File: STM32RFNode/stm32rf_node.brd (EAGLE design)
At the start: 100 x 80 mm, 6 parts

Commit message: rounting step 1
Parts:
- U$2: value NRF24L01+REFDESIGN -> NRF24L01+REFDESIGNMINI; device nRF24L01+RefDesign:NRF24L01+REFDESIGN -> nRF24L01+RefDesign:NRF24L01+REFDESIGN-MINI
- moved U$5 24.3 mm to (47.0, 11.4), flipped to the bottom, turned to 270 degrees
- moved U$4 23.4 mm to (22.9, 8.89), flipped to the bottom, turned to 270 degrees
- moved U$3 23.3 mm to (38.1, 8.89), flipped to the bottom, turned to 270 degrees
- moved U$2 4.02 mm to (12.7, 10.2)
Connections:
- new net INT: U$1.PB_0, U$4.INT
- new net N$11: U$1.PC_15, U$2.3
- net N$1: now also U$1.PA_7, U$2.6; no longer U$1.PB_14, U$2.7
- net N$2: now also U$1.PA_6, U$2.7; no longer U$1.PB_15, U$2.6
- net N$3: now also U$1.PA_5; no longer U$1.PB_13
- net N$4: now also U$1.PA_4; no longer U$1.PB_12
- net N$5: now also U$1.PB_1, U$4.A0; no longer U$1.PA_8, U$2.3
- net N$6: now also U$1.PA_0; no longer U$1.PA_9
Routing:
- net GND: track 0.00 -> 58.9 mm
- net N$5: track 0.00 -> 13.3 mm
- net N$3: track 0.00 -> 13.2 mm
- net 3V3: track 0.00 -> 11.2 mm
- net 5V: track 0.00 -> 8.67 mm
- net INT: track 0.00 -> 6.17 mm
- net N$6: track 0.00 -> 5.08 mm
- net N$8: track 0.00 -> 2.54 mm
- net N$7: track 0.00 -> 2.54 mm

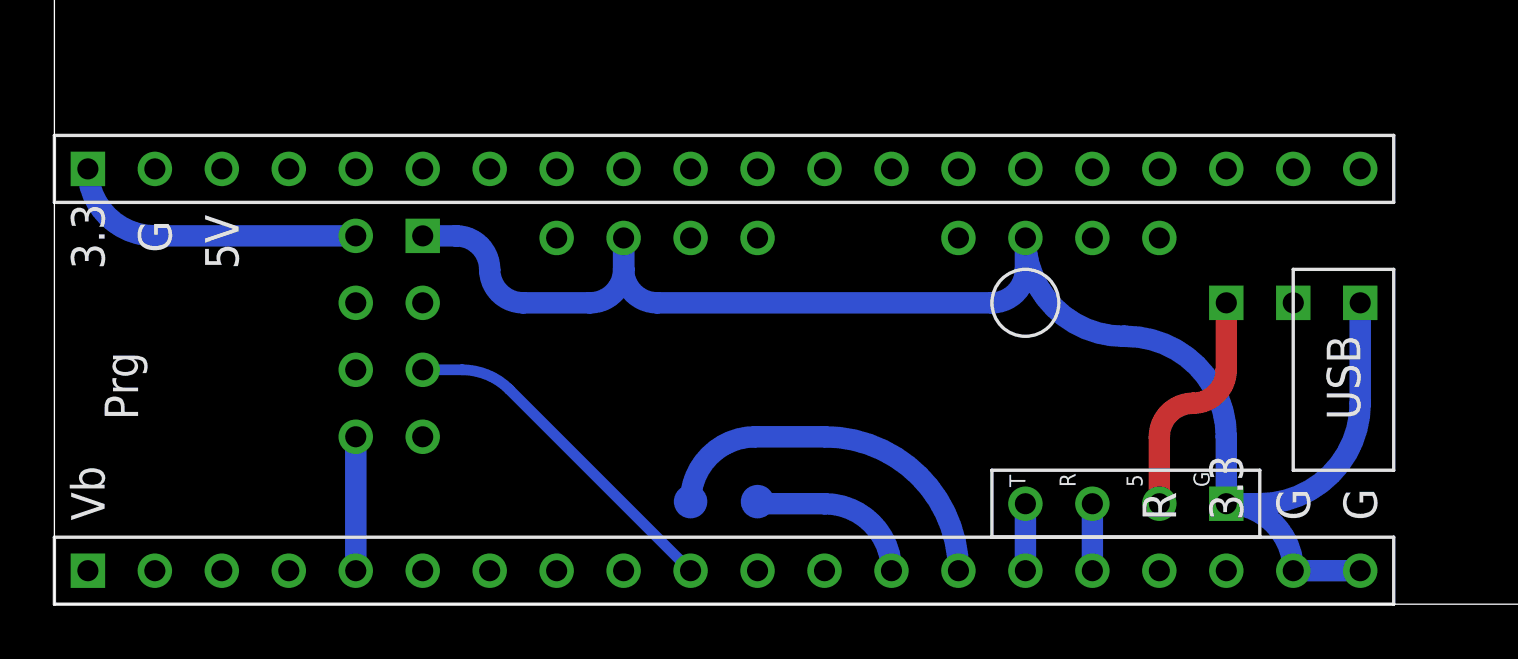
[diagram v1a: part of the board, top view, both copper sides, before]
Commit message: done routing with gnd rastnet
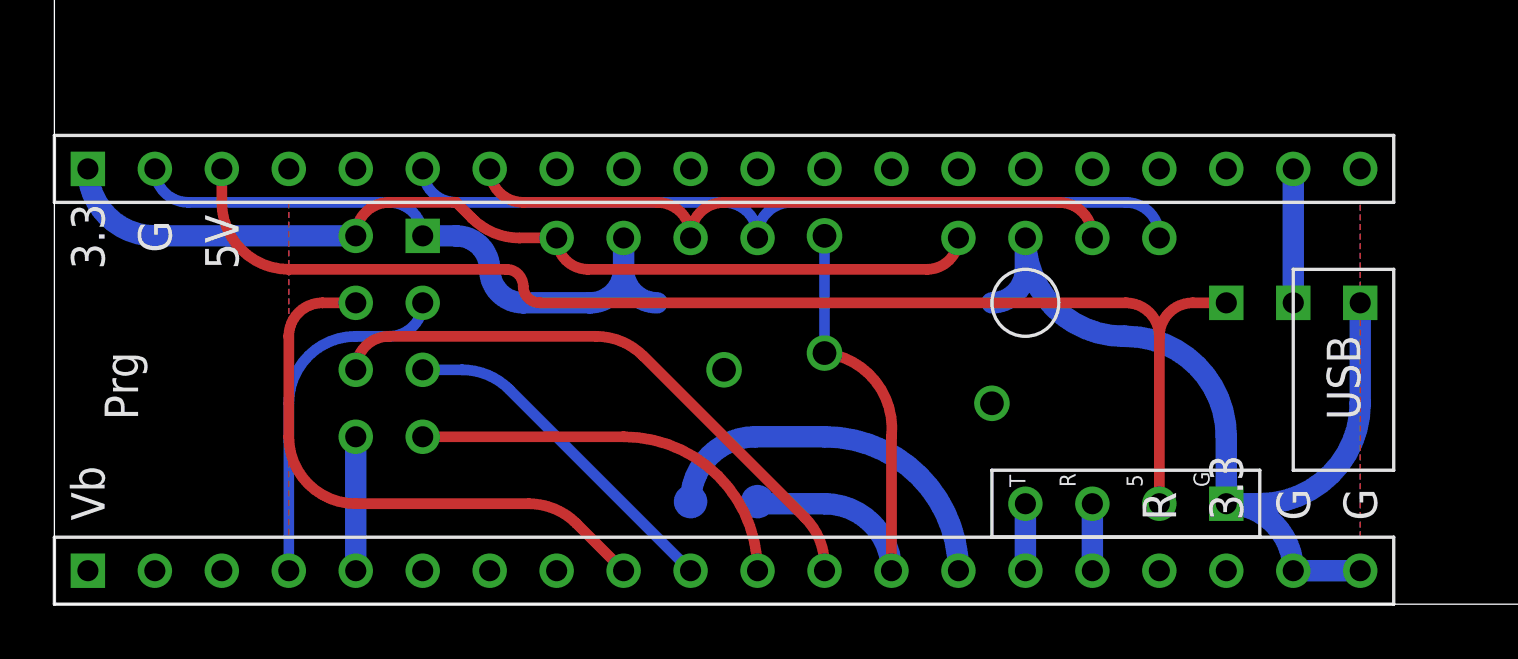
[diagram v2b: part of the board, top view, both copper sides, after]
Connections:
- new net N$12: U$1.PB_13, U$5.S
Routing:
- net 5V: track 8.67 -> 48.4 mm
- net N$10: track 0.00 -> 30.3 mm
- net N$9: track 0.00 -> 25.2 mm
- net 3V3: track 11.2 -> 36.0 mm
- net N$1: track 0.00 -> 22.4 mm
- net N$4: track 0.00 -> 21.5 mm
- net N$2: track 0.00 -> 14.8 mm
- net INT: track 6.17 -> 19.8 mm, vias 0 -> 2
- net N$11: track 0.00 -> 13.0 mm
- net N$12: track 0.00 -> 5.08 mm
- net GND: track 58.9 -> 56.3 mm, vias 0 -> 2
- added copper zone on layer 1, net GND
- added copper zone on layer 16, net GND
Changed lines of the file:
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@@
 <wire x1="36.83" y1="13.89" x2="36.83" y2="12.7" width="0.8128" layer="16"/>
 <wire x1="36.83" y1="12.7" x2="35.56" y2="11.43" width="0.8128" layer="16" curve="-90"/>
-<wire x1="35.56" y1="11.43" x2="22.86" y2="11.43" width="0.8128" layer="16"/>
 <wire x1="22.86" y1="11.43" x2="21.59" y2="12.7" width="0.8128" layer="16" curve="-90"/>
-<wire x1="21.59" y1="12.7" x2="21.59" y2="13.89" width="0.8128" layer="16"/>
 <wire x1="21.59" y1="13.89" x2="21.59" y2="12.7" width="0.8128" layer="16"/>
 <wire x1="21.59" y1="12.7" x2="20.32" y2="11.43" width="0.8128" layer="16" curve="-90"/>
@@
 <wire x1="16.51" y1="12.7" x2="15.24" y2="13.97" width="0.8128" layer="16" curve="90"/>
 <wire x1="15.24" y1="13.97" x2="13.97" y2="13.97" width="0.8128" layer="16"/>
-<wire x1="3.81" y1="16.51" x2="13.97" y2="13.97" width="0" layer="19" extent="1-1"/>
+<wire x1="13.97" y1="13.97" x2="12.7" y2="15.24" width="0.4064" layer="16" curve="90"/>
+<wire x1="12.7" y1="15.24" x2="5.08" y2="15.24" width="0.4064" layer="16"/>
+<wire x1="5.08" y1="15.24" x2="3.81" y2="16.51" width="0.4064" layer="16" curve="-90"/>
+<polygon width="0.4064" layer="16" isolate="0.8128">
+<vertex x="8.89" y="15.24"/>
+<vertex x="8.89" y="2.54"/>
+<vertex x="49.53" y="2.54"/>
+<vertex x="49.53" y="15.24"/>
+</polygon>
+<polygon width="0.4064" layer="1" isolate="0.8128">
+<vertex x="8.89" y="15.24"/>
+<vertex x="8.89" y="2.54"/>
+<vertex x="49.53" y="2.54"/>
+<vertex x="49.53" y="15.24"/>
+</polygon>
+<via x="35.56" y="7.62" extent="1-16" drill="0.9"/>
+<via x="25.4" y="8.89" extent="1-16" drill="0.9"/>
 </signal>
 <signal name="3V3">
@@
 <wire x1="11.43" y1="13.97" x2="3.81" y2="13.97" width="0.8128" layer="16"/>
 <wire x1="3.81" y1="13.97" x2="1.27" y2="16.51" width="0.8128" layer="16" curve="-90"/>
-<wire x1="19.05" y1="13.89" x2="34.29" y2="13.89" width="0" layer="19" extent="1-1"/>
-<wire x1="11.43" y1="13.97" x2="19.05" y2="13.89" width="0" layer="19" extent="1-1"/>
+<wire x1="11.43" y1="13.97" x2="12.7" y2="15.24" width="0.4064" layer="1" curve="-90"/>
+<wire x1="12.7" y1="15.24" x2="15.24" y2="15.24" width="0.4064" layer="1"/>
+<wire x1="15.24" y1="15.24" x2="15.84605" y2="14.63395" width="0.4064" layer="1"/>
+<wire x1="15.84605" y1="14.63395" x2="17.642103125" y2="13.89" width="0.4064" layer="1" curve="45.00007"/>
+<wire x1="17.642103125" y1="13.89" x2="19.05" y2="13.89" width="0.4064" layer="1"/>
+<wire x1="19.05" y1="13.89" x2="20.24" y2="12.7" width="0.4064" layer="1" curve="90"/>
+<wire x1="33.1" y1="12.7" x2="34.29" y2="13.89" width="0.4064" layer="1" curve="90"/>
+<wire x1="20.24" y1="12.7" x2="33.1" y2="12.7" width="0.4064" layer="1"/>
 </signal>
 <signal name="5V">
@@
 <contactref element="U$6" pad="2"/>
 <contactref element="U$1" pad="5V"/>
-<wire x1="41.91" y1="3.81" x2="41.91" y2="6.35" width="0.8128" layer="1"/>
-<wire x1="41.91" y1="6.35" x2="43.18" y2="7.62" width="0.8128" layer="1" curve="-90"/>
-<wire x1="43.18" y1="7.62" x2="44.45" y2="8.89" width="0.8128" layer="1" curve="90"/>
-<wire x1="44.45" y1="8.89" x2="44.45" y2="11.43" width="0.8128" layer="1"/>
-<wire x1="6.35" y1="16.51" x2="41.91" y2="6.35" width="0" layer="19" extent="1-1"/>
+<wire x1="44.45" y1="11.43" x2="43.18" y2="11.43" width="0.4064" layer="1"/>
+<wire x1="43.18" y1="11.43" x2="41.91" y2="10.16" width="0.4064" layer="1" curve="90"/>
+<wire x1="41.91" y1="10.16" x2="41.91" y2="3.81" width="0.4064" layer="1"/>
+<wire x1="41.91" y1="10.16" x2="40.64" y2="11.43" width="0.4064" layer="1" curve="90"/>
+<wire x1="18.415" y1="11.43" x2="17.78" y2="12.065" width="0.4064" layer="1" curve="-90"/>
+<wire x1="17.78" y1="12.065" x2="17.145" y2="12.7" width="0.4064" layer="1" curve="90"/>
+<wire x1="8.89" y1="12.7" x2="6.35" y2="15.24" width="0.4064" layer="1" curve="-90"/>
+<wire x1="6.35" y1="15.24" x2="6.35" y2="16.51" width="0.4064" layer="1"/>
+<wire x1="40.64" y1="11.43" x2="18.415" y2="11.43" width="0.4064" layer="1"/>
+<wire x1="17.145" y1="12.7" x2="8.89" y2="12.7" width="0.4064" layer="1"/>
 </signal>
 <signal name="N$7">
@@
 <contactref element="U$1" pad="PB_6"/>
 <contactref element="U$4" pad="SCL"/>
-<wire x1="24.13" y1="13.89" x2="39.37" y2="13.89" width="0" layer="19" extent="1-1"/>
-<wire x1="16.51" y1="16.51" x2="39.37" y2="13.89" width="0" layer="19" extent="1-1"/>
+<wire x1="16.51" y1="16.51" x2="17.78" y2="15.24" width="0.4064" layer="1" curve="90"/>
+<wire x1="17.78" y1="15.24" x2="22.86" y2="15.24" width="0.4064" layer="1"/>
+<wire x1="22.86" y1="15.24" x2="24.13" y2="13.97" width="0.4064" layer="1" curve="-90"/>
+<wire x1="24.13" y1="13.97" x2="24.13" y2="13.89" width="0.4064" layer="1"/>
+<wire x1="24.13" y1="13.89" x2="24.13" y2="13.97" width="0.4064" layer="1"/>
+<wire x1="24.13" y1="13.97" x2="25.4" y2="15.24" width="0.4064" layer="1" curve="-90"/>
+<wire x1="25.4" y1="15.24" x2="38.1" y2="15.24" width="0.4064" layer="1"/>
+<wire x1="38.1" y1="15.24" x2="39.37" y2="13.97" width="0.4064" layer="1" curve="-90"/>
+<wire x1="39.37" y1="13.97" x2="39.37" y2="13.89" width="0.4064" layer="1"/>
 </signal>
 <signal name="N$10">
@@
 <contactref element="U$1" pad="PB_7"/>
 <contactref element="U$4" pad="SDA"/>
-<wire x1="26.67" y1="13.89" x2="41.91" y2="13.89" width="0" layer="19" extent="1-1"/>
-<wire x1="13.97" y1="16.51" x2="41.91" y2="13.89" width="0" layer="19" extent="1-1"/>
+<wire x1="13.97" y1="16.51" x2="15.24" y2="15.24" width="0.4064" layer="16" curve="90"/>
+<wire x1="15.24" y1="15.24" x2="25.4" y2="15.24" width="0.4064" layer="16"/>
+<wire x1="25.4" y1="15.24" x2="26.67" y2="13.97" width="0.4064" layer="16" curve="-90"/>
+<wire x1="26.67" y1="13.97" x2="26.67" y2="13.89" width="0.4064" layer="16"/>
+<wire x1="26.67" y1="13.89" x2="26.67" y2="13.97" width="0.4064" layer="16"/>
+<wire x1="26.67" y1="13.97" x2="27.94" y2="15.24" width="0.4064" layer="16" curve="-90"/>
+<wire x1="27.94" y1="15.24" x2="40.64" y2="15.24" width="0.4064" layer="16"/>
+<wire x1="40.64" y1="15.24" x2="41.91" y2="13.97" width="0.4064" layer="16" curve="-90"/>
+<wire x1="41.91" y1="13.97" x2="41.91" y2="13.89" width="0.4064" layer="16"/>
 </signal>
 <signal name="N$1">
 <contactref element="U$2" pad="6"/>
 <contactref element="U$1" pad="PA_7"/>
-<wire x1="11.43" y1="8.89" x2="29.21" y2="1.27" width="0" layer="19" extent="1-1"/>
+<wire x1="12.7" y1="10.16" x2="11.43" y2="8.89" width="0.4064" layer="1" curve="90"/>
+<wire x1="29.21" y1="1.27" x2="29.21" y2="1.487896875" width="0.4064" layer="1"/>
+<wire x1="29.21" y1="1.487896875" x2="28.46605" y2="3.28395" width="0.4064" layer="1" curve="45.00005"/>
+<wire x1="22.33395" y1="9.41605" x2="20.537896875" y2="10.16" width="0.4064" layer="1" curve="45.00007"/>
+<wire x1="28.46605" y1="3.28395" x2="22.33395" y2="9.41605" width="0.4064" layer="1"/>
+<wire x1="20.537896875" y1="10.16" x2="12.7" y2="10.16" width="0.4064" layer="1"/>
 </signal>
 <signal name="N$2">
 <contactref element="U$2" pad="7"/>
 <contactref element="U$1" pad="PA_6"/>
-<wire x1="13.97" y1="6.35" x2="26.67" y2="1.27" width="0" layer="19" extent="1-1"/>
+<wire x1="26.67" y1="1.27" x2="21.59" y2="6.35" width="0.4064" layer="1" curve="90"/>
+<wire x1="21.59" y1="6.35" x2="13.97" y2="6.35" width="0.4064" layer="1"/>
 </signal>
 <signal name="N$3">
@@
 <contactref element="U$1" pad="PA_4"/>
 <contactref element="U$2" pad="4"/>
-<wire x1="11.43" y1="11.43" x2="21.59" y2="1.27" width="0" layer="19" extent="1-1"/>
+<wire x1="21.59" y1="1.27" x2="19.79395" y2="3.06605" width="0.4064" layer="1"/>
+<wire x1="19.79395" y1="3.06605" x2="17.997896875" y2="3.81" width="0.4064" layer="1" curve="45.00007"/>
+<wire x1="17.997896875" y1="3.81" x2="11.43" y2="3.81" width="0.4064" layer="1"/>
+<wire x1="11.43" y1="3.81" x2="8.89" y2="6.35" width="0.4064" layer="1" curve="-90"/>
+<wire x1="8.89" y1="6.35" x2="8.89" y2="10.16" width="0.4064" layer="1"/>
+<wire x1="8.89" y1="10.16" x2="10.16" y2="11.43" width="0.4064" layer="1" curve="-90"/>
+<wire x1="10.16" y1="11.43" x2="11.43" y2="11.43" width="0.4064" layer="1"/>
 </signal>
 <signal name="INT">
@@
 <wire x1="29.21" y1="3.81" x2="26.75" y2="3.81" width="0.8128" layer="16"/>
 <wire x1="26.75" y1="3.81" x2="26.67" y2="3.89" width="0.8128" layer="16" curve="-90"/>
+<via x="29.21" y="13.97" extent="1-16" drill="0.9"/>
+<wire x1="29.21" y1="13.97" x2="29.21" y2="9.525" width="0.4064" layer="16"/>
+<via x="29.21" y="9.525" extent="1-16" drill="0.9"/>
+<wire x1="29.21" y1="9.525" x2="31.75" y2="6.35" width="0.4064" layer="1" curve="-90"/>
+<wire x1="31.75" y1="6.35" x2="31.75" y2="1.27" width="0.4064" layer="1"/>
 </signal>
 <signal name="N$5">
@@
 <contactref element="U$1" pad="PC_15"/>
 <contactref element="U$2" pad="3"/>
-<wire x1="8.89" y1="1.27" x2="13.97" y2="11.43" width="0" layer="19" extent="1-1"/>
+<wire x1="8.89" y1="1.27" x2="8.89" y2="7.62" width="0.4064" layer="16"/>
+<wire x1="8.89" y1="7.62" x2="11.43" y2="10.16" width="0.4064" layer="16" curve="-90"/>
+<wire x1="11.43" y1="10.16" x2="12.7" y2="10.16" width="0.4064" layer="16"/>
+<wire x1="12.7" y1="10.16" x2="13.97" y2="11.43" width="0.4064" layer="16" curve="90"/>
+</signal>
+<signal name="N$12">
+<contactref element="U$1" pad="PB_13"/>
+<contactref element="U$5" pad="S"/>
+<wire x1="46.99" y1="16.51" x2="46.99" y2="11.43" width="0.8128" layer="16"/>
 </signal>
 </signals>
